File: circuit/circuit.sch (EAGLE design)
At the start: 15 parts, among them IC1 AT90S2313P, Q1 16MHz

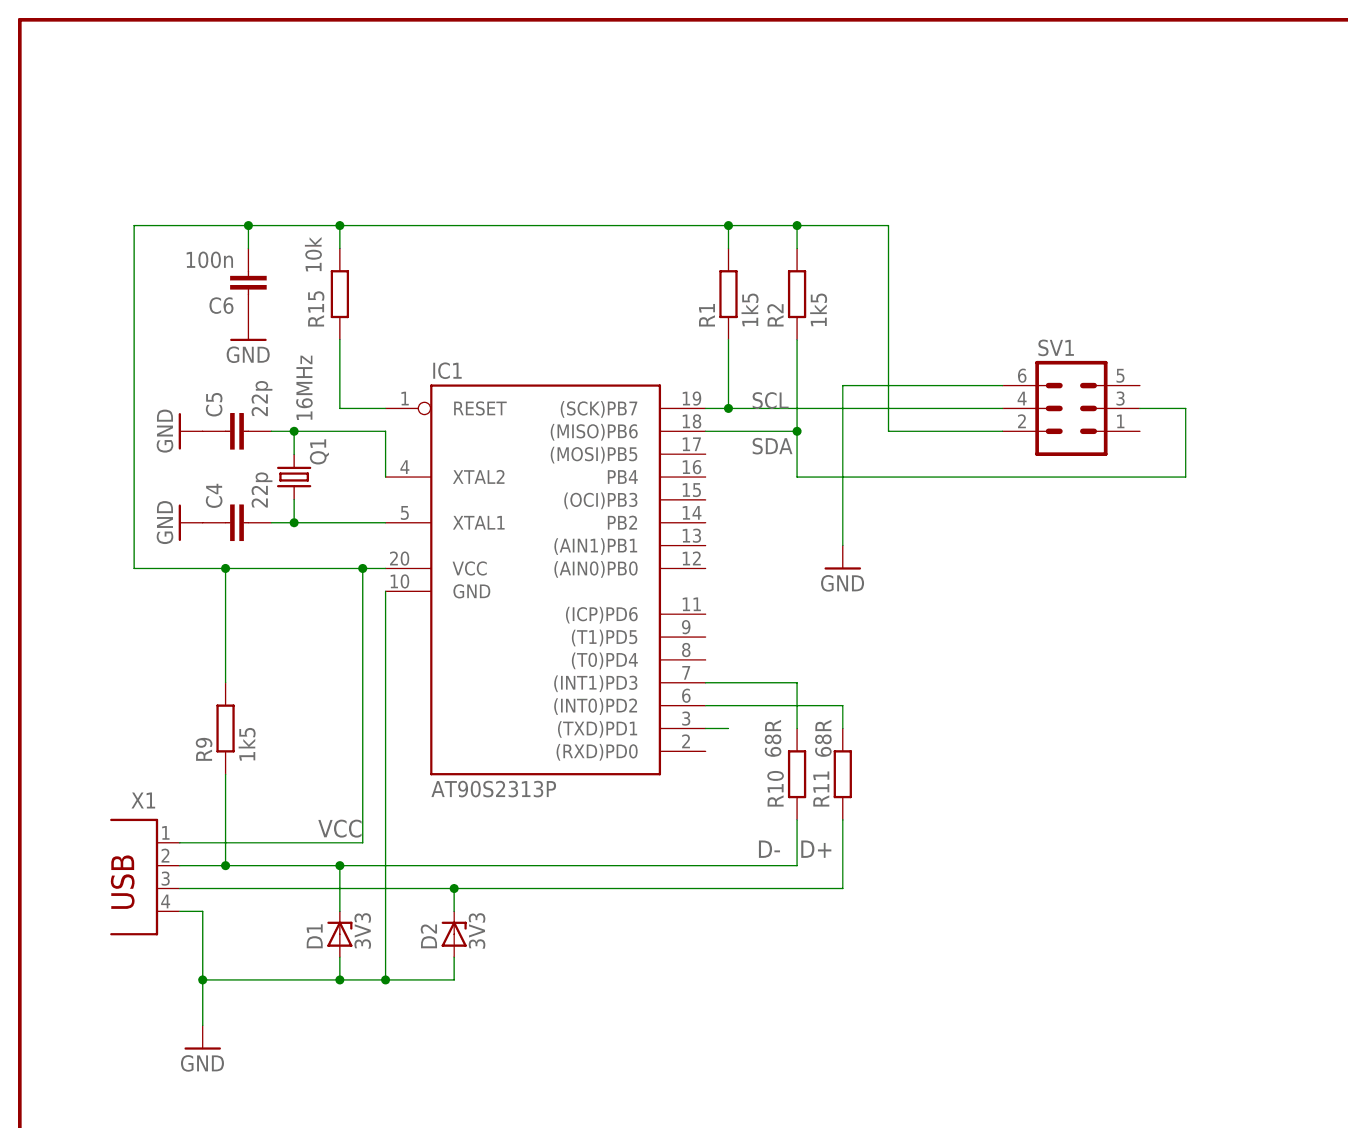
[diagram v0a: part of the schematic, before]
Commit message: circuit: start work on board layout
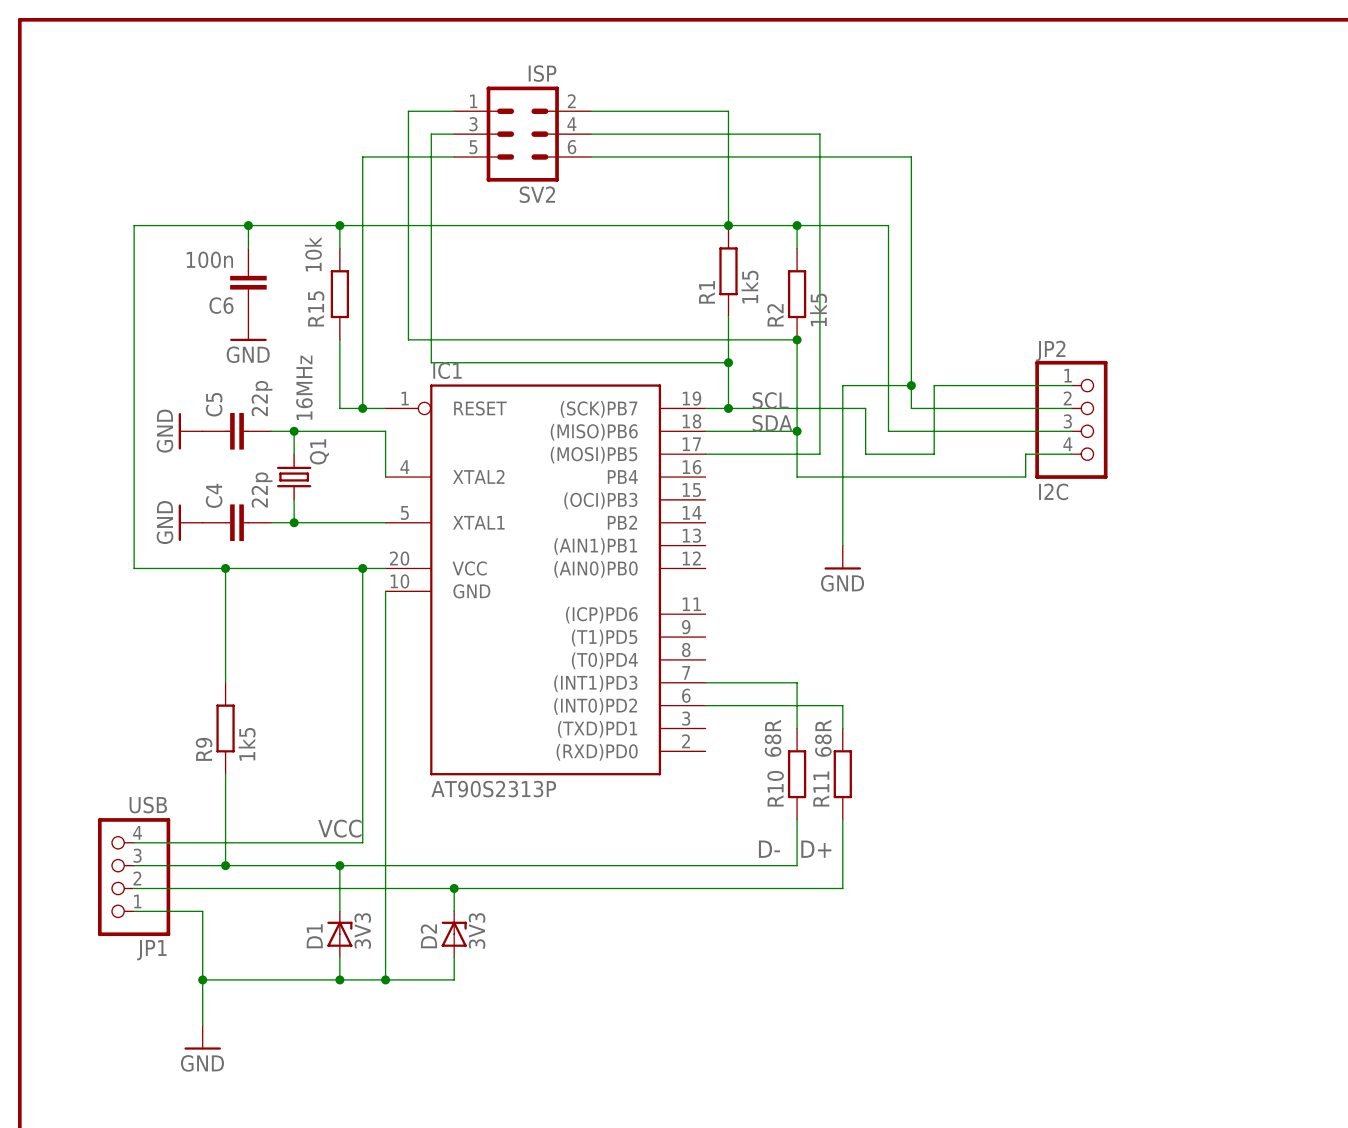
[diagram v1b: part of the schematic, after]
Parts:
- removed SV1: (no value), con-lstb:MA03-2
- removed X1: (no value), con-berg:PN61729
- added JP1: USB, pinhead:PINHD-1X4
- added JP2: I2C, pinhead:PINHD-1X4
- added SV2: ISP, con-harting-ml:ML6
- C4, C5, C6: device rcl:C-EU025-025X050 -> rcl:C-EUC0805
- R1, R2: device resistor:R-EU_0204/7 -> rcl:R-EU_0207/10
- R10, R11, R15, R9: device rcl:R-EU_0309/12 -> rcl:R-EU_0207/10
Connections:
- removed net N$45: IC1.(TXD)PD1
- new net N$4: IC1.(MOSI)PB5, SV2.4
- net D+: now also JP1.2; no longer X1.3
- net D-: now also JP1.3; no longer X1.2
- net GND: now also JP1.1, JP2.2, SV2.6; no longer SV1.6, X1.4
- net N$1: now also SV2.5
- net SCL: now also JP2.1, SV2.3; no longer SV1.4
- net SDA: now also JP2.4, SV2.1; no longer SV1.3
- net VCC: now also JP1.4, JP2.3, SV2.2; no longer SV1.2, X1.1
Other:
- moved on the sheet: R1

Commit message: such layout, wow
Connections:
- net GND: now also JP2.1; no longer JP2.2
- net SCL: now also JP2.2; no longer JP2.1
- net SDA: now also JP2.3; no longer JP2.4
- net VCC: now also JP2.4; no longer JP2.3
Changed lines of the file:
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@@
 <segment>
 <pinref part="GND1" gate="1" pin="GND"/>
-<wire x1="99.06" y1="139.7" x2="91.44" y2="139.7" width="0.1524" layer="91"/>
+<wire x1="91.44" y1="165.1" x2="91.44" y2="139.7" width="0.1524" layer="91"/>
+<pinref part="SV2" gate="1" pin="6"/>
 <wire x1="91.44" y1="139.7" x2="91.44" y2="121.92" width="0.1524" layer="91"/>
-<pinref part="SV2" gate="1" pin="6"/>
-<wire x1="63.5" y1="165.1" x2="99.06" y2="165.1" width="0.1524" layer="91"/>
-<wire x1="99.06" y1="165.1" x2="99.06" y2="139.7" width="0.1524" layer="91"/>
-<pinref part="JP2" gate="A" pin="2"/>
-<wire x1="116.84" y1="137.16" x2="99.06" y2="137.16" width="0.1524" layer="91"/>
-<wire x1="99.06" y1="137.16" x2="99.06" y2="139.7" width="0.1524" layer="91"/>
-<junction x="99.06" y="139.7"/>
+<wire x1="63.5" y1="165.1" x2="91.44" y2="165.1" width="0.1524" layer="91"/>
+<pinref part="JP2" gate="A" pin="1"/>
+<wire x1="116.84" y1="139.7" x2="91.44" y2="139.7" width="0.1524" layer="91"/>
+<junction x="91.44" y="139.7"/>
 </segment>
 </net>
@@
 <wire x1="38.1" y1="88.9" x2="38.1" y2="119.38" width="0.1524" layer="91"/>
 <junction x="38.1" y="119.38"/>
-<wire x1="116.84" y1="134.62" x2="96.52" y2="134.62" width="0.1524" layer="91"/>
-<wire x1="96.52" y1="134.62" x2="96.52" y2="157.48" width="0.1524" layer="91"/>
-<wire x1="96.52" y1="157.48" x2="86.36" y2="157.48" width="0.1524" layer="91"/>
+<wire x1="104.14" y1="157.48" x2="86.36" y2="157.48" width="0.1524" layer="91"/>
 <junction x="35.56" y="157.48"/>
 <pinref part="R1" gate="G$1" pin="2"/>
@@
 <wire x1="63.5" y1="170.18" x2="78.74" y2="170.18" width="0.1524" layer="91"/>
 <wire x1="78.74" y1="170.18" x2="78.74" y2="157.48" width="0.1524" layer="91"/>
-<pinref part="JP2" gate="A" pin="3"/>
+<pinref part="JP2" gate="A" pin="4"/>
+<wire x1="116.84" y1="132.08" x2="104.14" y2="132.08" width="0.1524" layer="91"/>
+<wire x1="104.14" y1="132.08" x2="104.14" y2="157.48" width="0.1524" layer="91"/>
 </segment>
 </net>
@@
 <wire x1="45.72" y1="142.24" x2="78.74" y2="142.24" width="0.1524" layer="91"/>
 <junction x="78.74" y="142.24"/>
-<pinref part="JP2" gate="A" pin="1"/>
-<wire x1="116.84" y1="139.7" x2="101.6" y2="139.7" width="0.1524" layer="91"/>
-<wire x1="101.6" y1="139.7" x2="101.6" y2="132.08" width="0.1524" layer="91"/>
-<wire x1="101.6" y1="132.08" x2="93.98" y2="132.08" width="0.1524" layer="91"/>
-<wire x1="93.98" y1="132.08" x2="93.98" y2="137.16" width="0.1524" layer="91"/>
-<wire x1="93.98" y1="137.16" x2="78.74" y2="137.16" width="0.1524" layer="91"/>
 <junction x="78.74" y="137.16"/>
+<pinref part="JP2" gate="A" pin="2"/>
+<wire x1="116.84" y1="137.16" x2="78.74" y2="137.16" width="0.1524" layer="91"/>
 </segment>
 </net>
@@
 <pinref part="IC1" gate="G$1" pin="(MISO)PB6"/>
 <wire x1="76.2" y1="134.62" x2="86.36" y2="134.62" width="0.1524" layer="91"/>
-<wire x1="86.36" y1="134.62" x2="86.36" y2="129.54" width="0.1524" layer="91"/>
 <pinref part="R2" gate="G$1" pin="1"/>
 <wire x1="86.36" y1="134.62" x2="86.36" y2="144.78" width="0.1524" layer="91"/>
@@
 <wire x1="43.18" y1="144.78" x2="86.36" y2="144.78" width="0.1524" layer="91"/>
 <junction x="86.36" y="144.78"/>
-<wire x1="86.36" y1="129.54" x2="111.76" y2="129.54" width="0.1524" layer="91"/>
-<wire x1="111.76" y1="129.54" x2="111.76" y2="132.08" width="0.1524" layer="91"/>
-<pinref part="JP2" gate="A" pin="4"/>
-<wire x1="111.76" y1="132.08" x2="116.84" y2="132.08" width="0.1524" layer="91"/>
+<pinref part="JP2" gate="A" pin="3"/>
+<wire x1="116.84" y1="134.62" x2="86.36" y2="134.62" width="0.1524" layer="91"/>
 </segment>
 </net>

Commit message: more layouting
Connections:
- net N$27 renamed AVRD+
- net N$41 renamed AVRD-
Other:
- moved on the sheet: D1, D2, JP1, JP2, R1, R10, R11, R2, R9

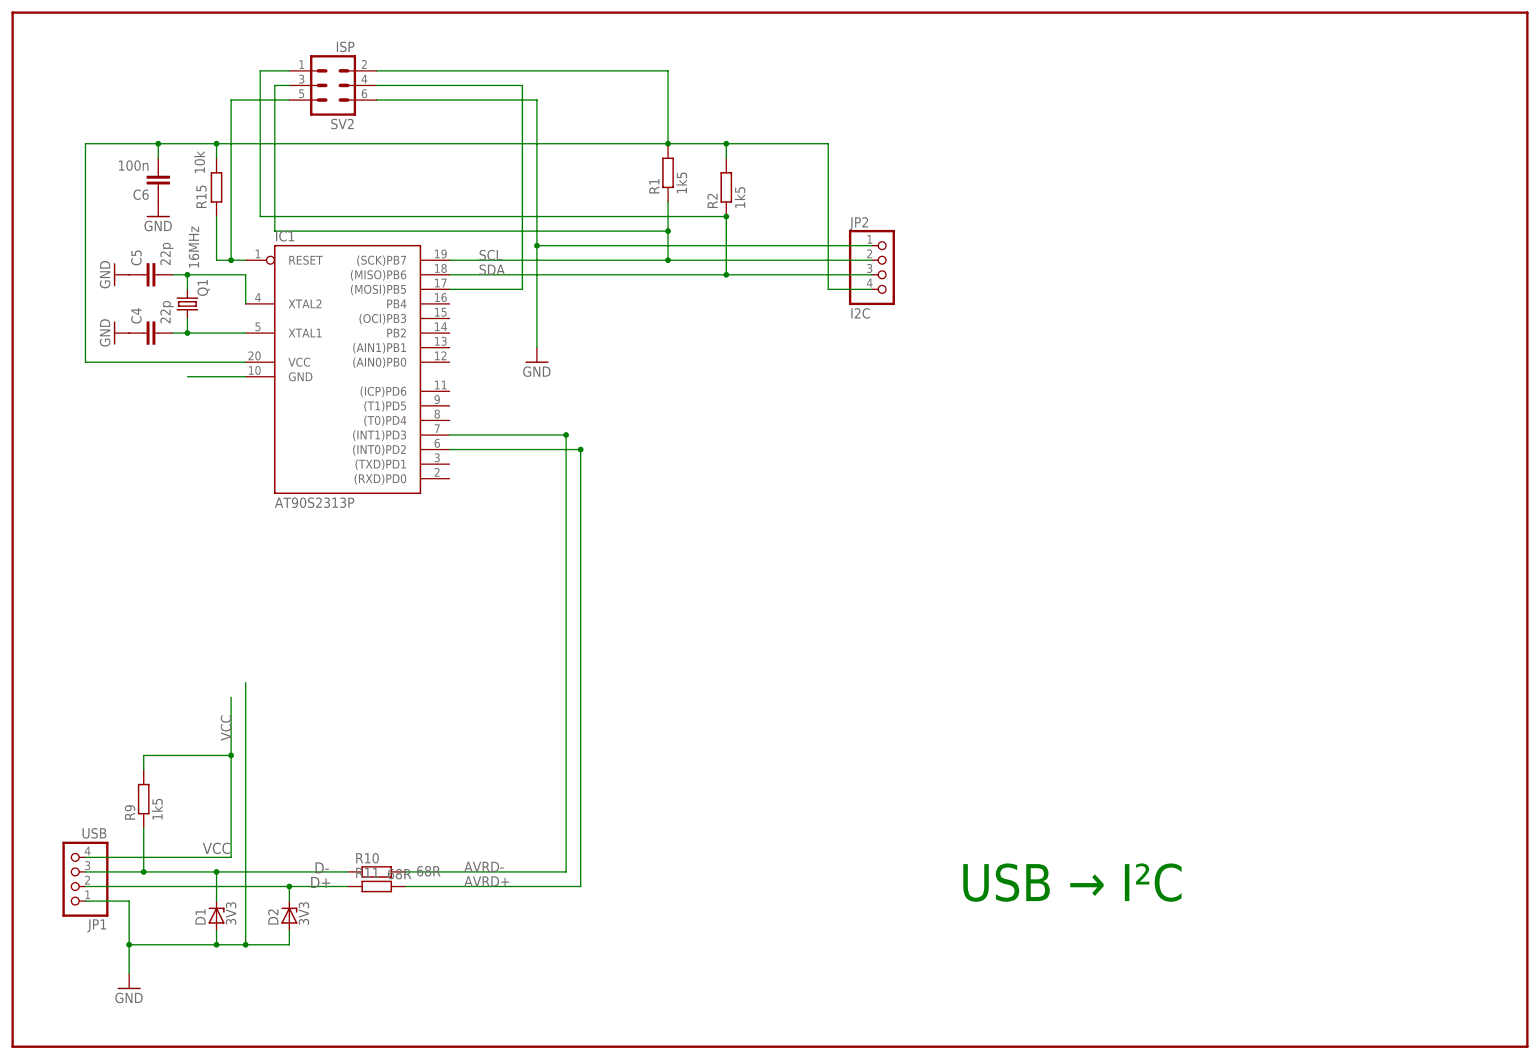
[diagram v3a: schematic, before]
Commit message: circuit: proper schematic
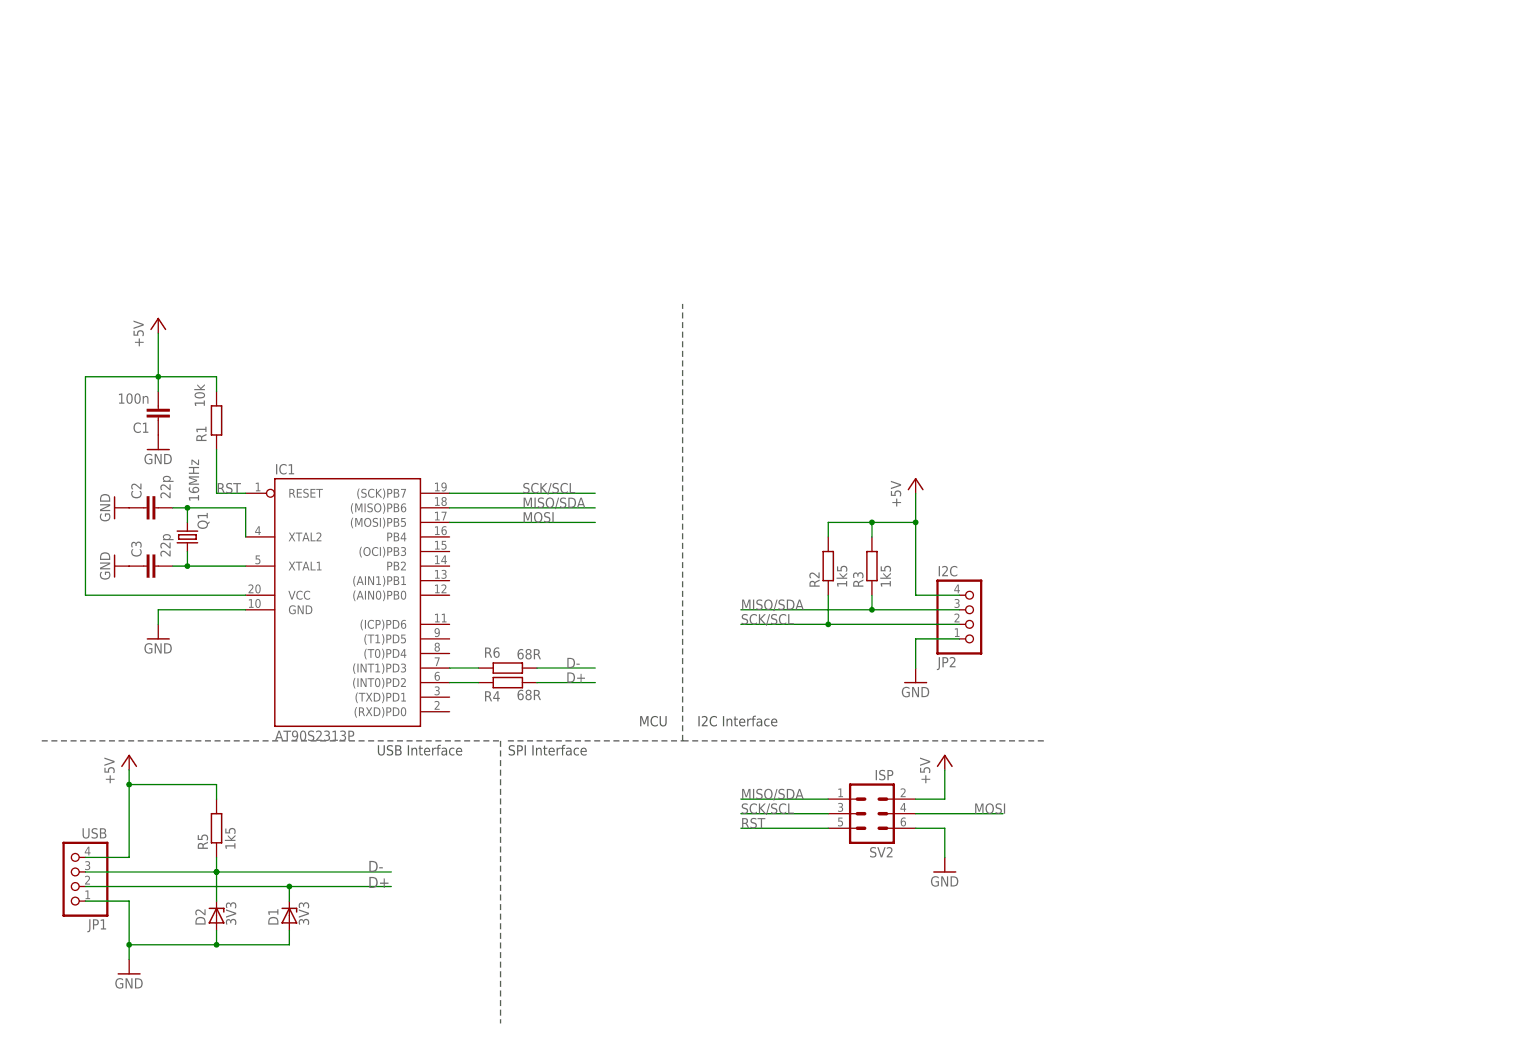
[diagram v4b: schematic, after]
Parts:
- removed C4, C5: 22p, rcl:C-EUC0805
- removed C6: 100n, rcl:C-EUC0805
- removed R10, R11: 68R, rcl:R-EU_0207/10
- removed R15: 10k, rcl:R-EU_0207/10
- removed R9: 1k5, rcl:R-EU_0207/10
- added C1: 100n, rcl:C-EUC0805
- added C2, C3: 22p, rcl:C-EUC0805
- added R3, R5: 1k5, rcl:R-EU_0207/10
- added R4, R6: 68R, rcl:R-EU_0207/10
- R1: value 1k5 -> 10k
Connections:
- net N$4 renamed MOSI
- removed net N$1: IC1.RESET, R15.1, SV2.5
- removed net SCL: IC1.(SCK)PB7, JP2.2, R1.1, SV2.3
- removed net SDA: IC1.(MISO)PB6, JP2.3, R2.1, SV2.1
- removed net VCC: C6.2, IC1.VCC, JP1.4, JP2.4, R1.2, R15.2, R2.2, R9.2, SV2.2
- new net +5V: C1.2, IC1.VCC, JP1.4, JP2.4, R1.2, R2.2, R3.2, R5.2, SV2.2
- new net MISO/SDA: IC1.(MISO)PB6, JP2.3, R3.1, SV2.1
- new net RST: IC1.RESET, R1.1, SV2.5
- new net SCK/SCL: IC1.(SCK)PB7, JP2.2, R2.1, SV2.3
- net AVRD+: now also R4.2; no longer R11.2
- net AVRD-: now also R6.2; no longer R10.2
- net D+: now also D1.C, R4.1; no longer D2.C, R11.1
- net D-: now also D2.C, R5.1, R6.1; no longer D1.C, R10.1, R9.1
- net GND: now also C1.1, C2.1, C3.1; no longer C4.1, C5.1, C6.1
- net N$37: now also C3.2; no longer C4.2
- net N$38: now also C2.2; no longer C5.2
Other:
- note added: "I2C Interface"
- note added: "MCU"
- note added: "SPI Interface"
- note added: "USB Interface"
- note removed: "USB → I²C"
- moved on the sheet: D1, D2, IC1, JP2, Q1, R1, R2, SV2
